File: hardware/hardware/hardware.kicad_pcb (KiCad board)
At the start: 2 copper layers, 123.7 x 113.1 mm, 25 parts, among them M1 Stepper_Motor_unipolar_5pin, M2 Stepper_Motor_unipolar_5pin, M3 Stepper_Motor_unipolar_5pin, SW1 SW_Push_SPDT, SW10 SW_Push_SPDT, SW11 SW_Push_SPDT, SW12 SW_Push_SPDT, SW13 SW_Push_SPDT, SW14 SW_Push_SPDT, SW15 SW_Push_SPDT, SW16 SW_Push_SPDT, SW2 SW_Push_SPDT, SW3 SW_Push_SPDT, SW4 SW_Push_SPDT, SW5 SW_Push_SPDT, SW6 SW_Push_SPDT, SW7 SW_Push_SPDT, SW8 SW_Push_SPDT, SW9 SW_Push_SPDT, U1 WeMos_D1_mini, U2 CD4051B, U3 CD4051B, U4 ULN2003A, U5 ULN2003A, U6 ULN2003A

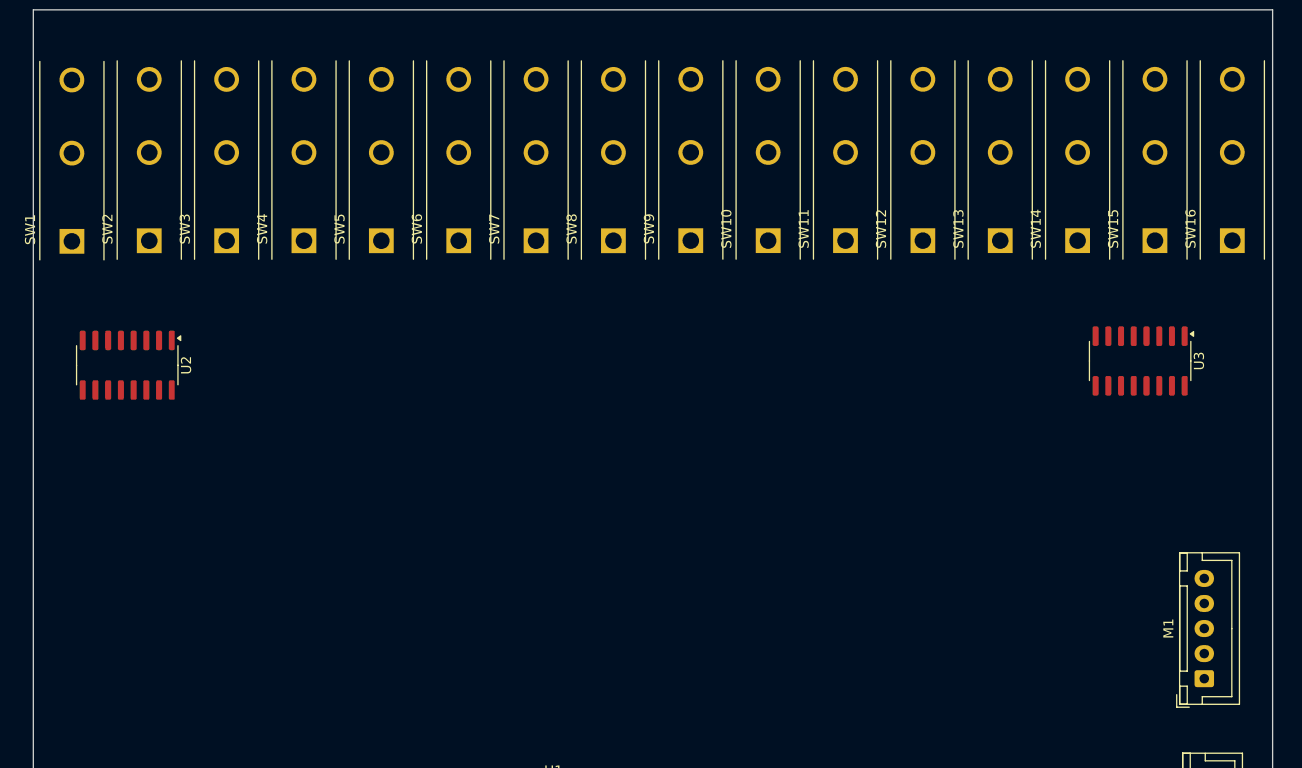
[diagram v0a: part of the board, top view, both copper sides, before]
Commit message: added continuous rotation to stepper
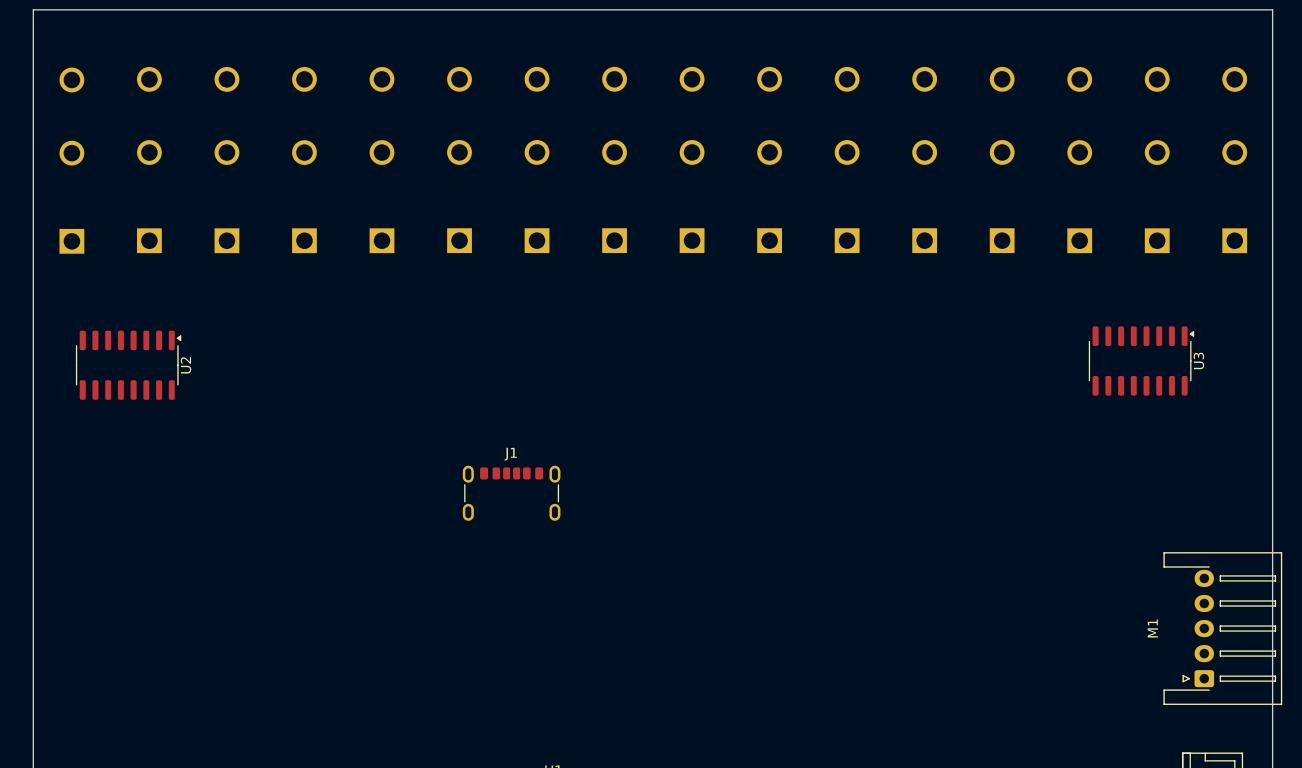
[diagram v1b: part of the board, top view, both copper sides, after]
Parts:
- added J1: USB_C_Receptacle_PowerOnly_6P, Connector_USB:USB_C_Receptacle_GCT_USB4125-xx-x-0190_6P_TopMnt_Horizontal, F.Cu at (89.6, 91.7)
- M1: footprint Connector_JST:JST_XH_B5B-XH-A_1x05_P2.50mm_Vertical -> Connector_JST:JST_XH_S5B-XH-A-1_1x05_P2.50mm_Horizontal
- SW1, SW10, SW11, SW12, SW13, SW14, SW15, SW16, SW2, SW3, SW4, SW5, SW6, SW7, SW8, SW9: moved to B.Cu
- moved SW6 77.4 mm to (161.7, 65.4)
- moved SW16 77.1 mm to (84.4, 65.4)
- moved SW7 62.0 mm to (154.0, 65.4)
- moved SW15 61.7 mm to (92.1, 65.4)
- moved SW8 46.5 mm to (146.3, 65.4)
- moved SW14 46.2 mm to (99.9, 65.4)
- moved SW9 31.1 mm to (138.5, 65.4)
- moved SW13 30.8 mm to (107.6, 65.4)
- moved SW10 15.6 mm to (130.8, 65.4)
- moved SW12 15.3 mm to (115.3, 65.4)
- moved SW4 7.78 mm to (76.6, 65.4)
- moved SW5 7.67 mm to (68.9, 65.4)
- moved SW11 0.16 mm to (123.1, 65.4)

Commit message: added final pcb design
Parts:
- added C1: 10pF, Capacitor_SMD:C_0805_2012Metric, F.Cu at (98.0, 162.7)
- added C10: 10pF, Capacitor_SMD:C_0805_2012Metric, F.Cu at (102.4, 174.8)
- added C11: 10pF, Capacitor_SMD:C_0805_2012Metric, F.Cu at (106.9, 162.7)
- added C12: 10pF, Capacitor_SMD:C_0805_2012Metric, F.Cu at (106.9, 165.7)
- added C13: 10pF, Capacitor_SMD:C_0805_2012Metric, F.Cu at (106.9, 168.8)
- added C14: 10pF, Capacitor_SMD:C_0805_2012Metric, F.Cu at (106.9, 171.8)
- added C2: 10pF, Capacitor_SMD:C_0805_2012Metric, F.Cu at (98.0, 165.7)
- added C3: 10pF, Capacitor_SMD:C_0805_2012Metric, F.Cu at (98.0, 168.8)
- added C4: 10pF, Capacitor_SMD:C_0805_2012Metric, F.Cu at (98.0, 171.8)
- added C5: 10pF, Capacitor_SMD:C_0805_2012Metric, F.Cu at (98.0, 174.8)
- added C6: 10pF, Capacitor_SMD:C_0805_2012Metric, F.Cu at (102.4, 162.7)
- added C7: 10pF, Capacitor_SMD:C_0805_2012Metric, F.Cu at (102.4, 165.7)
- added C8: 10pF, Capacitor_SMD:C_0805_2012Metric, F.Cu at (102.4, 168.8)
- added C9: 10pF, Capacitor_SMD:C_0805_2012Metric, F.Cu at (102.4, 171.8)
- added J2: Barrel_Jack, Connector_BarrelJack:BarrelJack_CUI_PJ-063AH_Horizontal, F.Cu at (68.0, 114.7)
- added M10: Stepper_Motor_unipolar_5pin, Connector_Audio:HOOYA-PJ-3505A_C19190915-Jack_3.5mm_PJ31060-I_Horizontal, F.Cu at (159.4, 83.2)
- added M11: Stepper_Motor_unipolar_5pin, Connector_Audio:HOOYA-PJ-3505A_C19190915-Jack_3.5mm_PJ31060-I_Horizontal, F.Cu at (151.8, 83.5)
- added M12: Stepper_Motor_unipolar_5pin, Connector_Audio:HOOYA-PJ-3505A_C19190915-Jack_3.5mm_PJ31060-I_Horizontal, F.Cu at (188.4, 99.6)
- added M13: Stepper_Motor_unipolar_5pin, Connector_Audio:HOOYA-PJ-3505A_C19190915-Jack_3.5mm_PJ31060-I_Horizontal, F.Cu at (151.5, 100.0)
- added M14: Stepper_Motor_unipolar_5pin, Connector_Audio:HOOYA-PJ-3505A_C19190915-Jack_3.5mm_PJ31060-I_Horizontal, F.Cu at (159.7, 116.2)
- added M4: Stepper_Motor_unipolar_5pin, Connector_Audio:HOOYA-PJ-3505A_C19190915-Jack_3.5mm_PJ31060-I_Horizontal, F.Cu at (79.1, 84.3)
- added M5: Stepper_Motor_unipolar_5pin, Connector_Audio:HOOYA-PJ-3505A_C19190915-Jack_3.5mm_PJ31060-I_Horizontal, F.Cu at (47.9, 91.0)
- added M6: Stepper_Motor_unipolar_5pin, Connector_Audio:HOOYA-PJ-3505A_C19190915-Jack_3.5mm_PJ31060-I_Horizontal, F.Cu at (56.5, 90.8)
- added M7: Stepper_Motor_unipolar_5pin, Connector_Audio:HOOYA-PJ-3505A_C19190915-Jack_3.5mm_PJ31060-I_Horizontal, F.Cu at (47.9, 107.2)
- added M8: Stepper_Motor_unipolar_5pin, Connector_Audio:HOOYA-PJ-3505A_C19190915-Jack_3.5mm_PJ31060-I_Horizontal, F.Cu at (159.3, 67.1)
- added M9: Stepper_Motor_unipolar_5pin, Connector_Audio:HOOYA-PJ-3505A_C19190915-Jack_3.5mm_PJ31060-I_Horizontal, F.Cu at (151.7, 67.5)
- added R1: 1K, Resistor_SMD:R_0805_2012Metric, F.Cu at (172.1, 129.5)
- added R10: 1K, Resistor_SMD:R_0805_2012Metric, F.Cu at (102.4, 159.8)
- added R11: 1K, Resistor_SMD:R_0805_2012Metric, F.Cu at (106.8, 148.0)
- added R12: 1K, Resistor_SMD:R_0805_2012Metric, F.Cu at (106.8, 150.9)
- added R13: 1K, Resistor_SMD:R_0805_2012Metric, F.Cu at (106.8, 153.9)
- added R14: 1K, Resistor_SMD:R_0805_2012Metric, F.Cu at (106.8, 156.8)
- added R15: 1K, Resistor_SMD:R_0805_2012Metric, F.Cu at (106.8, 159.8)
- added R16: 1K, Resistor_SMD:R_0805_2012Metric, F.Cu at (111.2, 148.0)
- added R17: 1K, Resistor_SMD:R_0805_2012Metric, F.Cu at (111.2, 150.9)
- added R18: 1K, Resistor_SMD:R_0805_2012Metric, F.Cu at (111.2, 153.9)
- added R19: 1K, Resistor_SMD:R_0805_2012Metric, F.Cu at (111.2, 156.8)
- added R2: 1K, Resistor_SMD:R_0805_2012Metric, F.Cu at (98.0, 150.9)
- added R20: 10K, Resistor_SMD:R_0805_2012Metric, F.Cu at (111.2, 159.8)
- added R3: 1K, Resistor_SMD:R_0805_2012Metric, F.Cu at (98.0, 153.9)
- added R4: 1K, Resistor_SMD:R_0805_2012Metric, F.Cu at (98.0, 156.8)
- added R5: 1K, Resistor_SMD:R_0805_2012Metric, F.Cu at (98.0, 159.8)
- added R6: 1K, Resistor_SMD:R_0805_2012Metric, F.Cu at (102.4, 148.0)
- added R7: 1K, Resistor_SMD:R_0805_2012Metric, F.Cu at (102.4, 150.9)
- added R8: 1K, Resistor_SMD:R_0805_2012Metric, F.Cu at (102.4, 153.9)
- added R9: 1K, Resistor_SMD:R_0805_2012Metric, F.Cu at (102.4, 156.8)
- added U10: ULN2003A, Package_SO:SOIC-16_3.9x9.9mm_P1.27mm, F.Cu at (140.4, 50.0)
- added U11: ULN2003A, Package_SO:SOIC-16_3.9x9.9mm_P1.27mm, F.Cu at (67.3, 21.1)
- added U12: ULN2003A, Package_SO:SOIC-16_3.9x9.9mm_P1.27mm, F.Cu at (80.2, 20.6)
- added U13: ULN2003A, Package_SO:SOIC-16_3.9x9.9mm_P1.27mm, F.Cu at (92.4, 20.4)
- added U14: ULN2003A, Package_SO:SOIC-16_3.9x9.9mm_P1.27mm, F.Cu at (105.0, 21.2)
- added U15: ULN2003A, Package_SO:SOIC-16_3.9x9.9mm_P1.27mm, F.Cu at (117.4, 20.6)
- added U16: ULN2003A, Package_SO:SOIC-16_3.9x9.9mm_P1.27mm, F.Cu at (129.6, 20.4)
- added U17: ULN2003A, Package_SO:SOIC-16_3.9x9.9mm_P1.27mm, F.Cu at (141.9, 19.7)
- added U7: ULN2003A, Package_SO:SOIC-16_3.9x9.9mm_P1.27mm, F.Cu at (104.4, 49.9)
- added U8: ULN2003A, Package_SO:SOIC-16_3.9x9.9mm_P1.27mm, F.Cu at (116.5, 49.9)
- added U9: ULN2003A, Package_SO:SOIC-16_3.9x9.9mm_P1.27mm, F.Cu at (128.7, 49.9)
- M1: footprint Connector_JST:JST_XH_S5B-XH-A-1_1x05_P2.50mm_Horizontal -> Connector_Audio:HOOYA-PJ-3505A_C19190915-Jack_3.5mm_PJ31060-I_Horizontal
- M2, M3: footprint Connector_JST:JST_XH_B5B-XH-A_1x05_P2.50mm_Vertical -> Connector_Audio:HOOYA-PJ-3505A_C19190915-Jack_3.5mm_PJ31060-I_Horizontal
- moved SW16 194.9 mm to (266.8, 134.0), turned to -90 degrees
- moved SW15 181.8 mm to (260.5, 134.0), turned to -90 degrees
- moved SW14 168.9 mm to (254.2, 134.0), turned to -90 degrees
- moved SW13 156.2 mm to (247.9, 134.0), turned to -90 degrees
- moved SW5 145.8 mm to (197.6, 134.0), turned to -90 degrees
- moved SW1 144.1 mm to (172.5, 134.0), turned to -90 degrees
- moved SW12 143.7 mm to (241.6, 134.0), turned to -90 degrees
- moved SW2 142.9 mm to (178.7, 134.0), turned to -90 degrees
- moved SW3 141.6 mm to (185.0, 134.0), turned to -90 degrees
- moved M3 134.5 mm to (47.5, 74.3), turned to -90 degrees
- moved SW4 133.6 mm to (191.3, 134.0), turned to -90 degrees
- moved SW11 131.6 mm to (235.3, 134.0), turned to -90 degrees
- moved SW10 119.8 mm to (229.0, 134.0), turned to -90 degrees
- moved M1 117.4 mm to (53.1, 57.7)
- moved M2 111.1 mm to (73.2, 58.5), turned to -90 degrees
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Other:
- board size 123.7 x 113.1 mm -> 123.4 x 109.1 mm
- board text added: "BIJNA ALLE MOTEREN ZIJN AAN ELKAAR< CONNECTIONS RENAMEN"

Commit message: updated pcb design
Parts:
- removed J1: USB_C_Receptacle_PowerOnly_6P, Connector_USB:USB_C_Receptacle_GCT_USB4125-xx-x-0190_6P_TopMnt_Horizontal
- removed R20: 10K, Resistor_SMD:R_0805_2012Metric
- R10, R11, R12, R13, R14, R15, R16, R17, R18, R19, R4, R5, R6, R7, R8, R9: value 1K -> 10K
- SW1, SW10, SW11, SW12, SW13, SW14, SW15, SW16, SW2, SW3, SW4, SW5, SW6, SW7, SW8, SW9: footprint MS0850502F030P1A:SW_MS0850502F030P1A -> MS0850502F030P1A:SW_MS0850502F030P1A-fixed
- moved U11 191.9 mm to (255.9, 56.8)
- moved C8 183.7 mm to (248.0, 56.7), turned to -90 degrees
- moved U12 182.0 mm to (255.9, 68.1)
- moved C9 178.7 mm to (247.9, 68.0), turned to -90 degrees
- moved U13 173.9 mm to (255.9, 79.5)
- moved C10 173.7 mm to (247.5, 79.2), turned to -90 degrees
- moved U14 166.3 mm to (255.9, 90.9)
- moved R2 165.6 mm to (233.5, 55.7), turned to 180 degrees
- moved U15 161.1 mm to (255.9, 102.8)
- moved R19 160.8 mm to (271.8, 149.2), turned to -90 degrees
- moved C11 158.1 mm to (247.5, 90.5), turned to -90 degrees
- moved U16 157.1 mm to (255.9, 113.7)
- moved C12 154.1 mm to (247.5, 102.7), turned to -90 degrees
- moved U17 153.7 mm to (255.9, 122.9)
- moved R18 152.5 mm to (261.9, 130.7)
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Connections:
- M10 pad 2: ORANGE2 -> ORANGE10
- M10 pad 3: PINK2 -> PINK10
- M10 pad 4: YELLOW2 -> YELLOW10
- M10 pad 5: BLUE2 -> BLUE10
- M11 pad 2: ORANGE3 -> ORANGE11
- M11 pad 3: PINK3 -> PINK11
- M11 pad 4: YELLOW3 -> YELLOW11
- M11 pad 5: BLUE3 -> BLUE11
- M12 pad 2: ORANGE3 -> ORANGE12
- M12 pad 3: PINK3 -> PINK12
- M12 pad 4: YELLOW3 -> YELLOW12
- M12 pad 5: BLUE3 -> BLUE12
- M13 pad 2: ORANGE3 -> ORANGE13
- M13 pad 3: PINK3 -> PINK13
- M13 pad 4: YELLOW3 -> YELLOW13
- M13 pad 5: BLUE3 -> BLUE13
- M14 pad 2: ORANGE3 -> ORANGE14
- M14 pad 3: PINK3 -> PINK14
- M14 pad 4: YELLOW3 -> YELLOW14
- M14 pad 5: BLUE3 -> BLUE14
- M4 pad 2: ORANGE3 -> ORANGE4
- M4 pad 3: PINK3 -> PINK4
- M4 pad 4: YELLOW3 -> YELLOW4
- M4 pad 5: BLUE3 -> BLUE4
- M5 pad 2: ORANGE1 -> ORANGE5
- M5 pad 3: PINK1 -> PINK5
- M5 pad 4: YELLOW1 -> YELLOW5
- M5 pad 5: BLUE1 -> BLUE5
- M6 pad 2: ORANGE2 -> ORANGE6
- M6 pad 3: PINK2 -> PINK6
- M6 pad 4: YELLOW2 -> YELLOW6
- M6 pad 5: BLUE2 -> BLUE6
- M7 pad 2: ORANGE3 -> ORANGE7
- M7 pad 3: PINK3 -> PINK7
- M7 pad 4: YELLOW3 -> YELLOW7
- M7 pad 5: BLUE3 -> BLUE7
- M8 pad 2: ORANGE3 -> ORANGE8
- M8 pad 3: PINK3 -> PINK8
- M8 pad 4: YELLOW3 -> YELLOW8
- M8 pad 5: BLUE3 -> BLUE8
- M9 pad 2: ORANGE1 -> ORANGE9
- M9 pad 3: PINK1 -> PINK9
- M9 pad 4: YELLOW1 -> YELLOW9
- M9 pad 5: BLUE1 -> BLUE9
- U10 pad 13: ORANGE3 -> ORANGE7
- U10 pad 14: YELLOW3 -> YELLOW7
- U10 pad 15: PINK3 -> PINK7
- U10 pad 16: BLUE3 -> BLUE7
- U11 pad 13: ORANGE3 -> ORANGE8
- U11 pad 14: YELLOW3 -> YELLOW8
- U11 pad 15: PINK3 -> PINK8
- U11 pad 16: BLUE3 -> BLUE8
- U12 pad 13: ORANGE1 -> ORANGE9
- U12 pad 14: YELLOW1 -> YELLOW9
- U12 pad 15: PINK1 -> PINK9
- U12 pad 16: BLUE1 -> BLUE9
- U13 pad 13: ORANGE2 -> ORANGE10
- U13 pad 14: YELLOW2 -> YELLOW10
- U13 pad 15: PINK2 -> PINK10
- U13 pad 16: BLUE2 -> BLUE10
- U14 pad 13: ORANGE3 -> ORANGE11
- U14 pad 14: YELLOW3 -> YELLOW11
- U14 pad 15: PINK3 -> PINK11
- U14 pad 16: BLUE3 -> BLUE11
- U15 pad 13: ORANGE3 -> ORANGE12
- U15 pad 14: YELLOW3 -> YELLOW12
- U15 pad 15: PINK3 -> PINK12
- U15 pad 16: BLUE3 -> BLUE12
- U16 pad 13: ORANGE3 -> ORANGE13
- U16 pad 14: YELLOW3 -> YELLOW13
- U16 pad 15: PINK3 -> PINK13
- U16 pad 16: BLUE3 -> BLUE13
- U17 pad 13: ORANGE3 -> ORANGE14
- U17 pad 14: YELLOW3 -> YELLOW14
- U17 pad 15: PINK3 -> PINK14
- U17 pad 16: BLUE3 -> BLUE14
- U7 pad 13: ORANGE3 -> ORANGE4
- U7 pad 14: YELLOW3 -> YELLOW4
- U7 pad 15: PINK3 -> PINK4
- U7 pad 16: BLUE3 -> BLUE4
- U8 pad 13: ORANGE1 -> ORANGE5
- U8 pad 14: YELLOW1 -> YELLOW5
- U8 pad 15: PINK1 -> PINK5
- U8 pad 16: BLUE1 -> BLUE5
- U9 pad 13: ORANGE2 -> ORANGE6
- U9 pad 14: YELLOW2 -> YELLOW6
- U9 pad 15: PINK2 -> PINK6
- U9 pad 16: BLUE2 -> BLUE6
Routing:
- net GND: track 0.00 -> 822.2 mm, vias 0 -> 22
- net RED: track 0.00 -> 778.0 mm, vias 0 -> 1
- net IN1: track 0.00 -> 232.0 mm, vias 0 -> 28
- net IN3: track 0.00 -> 230.5 mm, vias 0 -> 28
- net IN2: track 0.00 -> 230.3 mm, vias 0 -> 30
- net IN4: track 0.00 -> 229.4 mm, vias 0 -> 29
- net B: track 0.00 -> 158.9 mm, vias 0 -> 2
- net C: track 0.00 -> 151.6 mm, vias 0 -> 3
- net MUX2COM: track 0.00 -> 86.2 mm, vias 0 -> 2
- net A: track 0.00 -> 84.9 mm, vias 0 -> 2
- net SW16: track 0.00 -> 78.2 mm
- net MUX1COM: track 0.00 -> 75.5 mm, vias 0 -> 2
- net SW1: track 0.00 -> 68.7 mm, vias 0 -> 2
- net SW15: track 0.00 -> 68.4 mm
- net SW14: track 0.00 -> 58.2 mm, vias 0 -> 2
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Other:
- board text removed: "BIJNA ALLE MOTEREN ZIJN AAN ELKAAR< CONNECTIONS RENAMEN"
